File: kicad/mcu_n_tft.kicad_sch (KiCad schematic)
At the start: 14 parts, among them Q3 SS8050-G, Q4 SS8050-G, SW1 SW_MEC_5G, SW2 SW_MEC_5G, U4 ESP32-S3-Rx

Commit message: rework pcb
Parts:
- removed C10, C11, C12: 100n, Capacitor_SMD:C_0603_1608Metric, symbol Device:C
- removed Q3, Q4: SS8050-G, Package_TO_SOT_SMD:SOT-23, symbol z_ic:SS8050-G
- removed R28, R29, R32: 10k, Resistor_SMD:R_0603_1608Metric, symbol Device:R
- removed R30, R31, R33: 0R, Resistor_SMD:R_0603_1608Metric, symbol Device:R
- removed SW1, SW2: SW_MEC_5G, z_connector:PTS820J25MSMTRLFS, symbol z_connectors:SW_MEC_5G
- removed U4: ESP32-S3-Rx, z_ic:ESP32-S3-WROOM-1, symbol z_ic:ESP32-S3-Rx
- added J?: Conn_01x05, mylib_connector:Easy-On 51281-5, symbol Connector_Generic:Conn_01x05
- added J?: TC-2050, mylib_connector:TC-2050, symbol mylib_connectors:TC-2050
- added U4: BL654, mylib_ic:BL654, symbol mylib_ic:BL654
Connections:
- net +3V3: now also J?.1 (VCC), U4.25 (VDD_HV), U4.31 (VDD)
- net GND: now also J?.3 (GND), J?.5 (GND), U4.0 (GND), U4.23 (GND), U4.26 (GND), U4.33 (GND), U4.40 (GND), U4.43 (GND), U4.47 (GND), U4.52 (GND), U4.55 (GND), U4.58 (GND), U4.65 (GND), U4.66 (GND), U4.67 (GND), U4.68 (GND), U4.69 (GND), U4.70 (GND), U4.71 (GND)
- net PWR_PWM: now also U4.6 (P1.01)
- net PWR_PWM_INT: now also U4.5 (P1.03)
- net SCL: now also U4.2 (P1.04)
- net SDA: now also U4.4 (P1.02)
- net ~{INT}: now also U4.27 (P0.11)
- net ~{PD}: now also U4.22 (P0.14)
- new net: J?.2 (Pin_2), U4.59 (NFC_1)
- new net: J?.4 (Pin_4), U4.57 (NFC_2)
- new net +5V: U4.24 (VBUS)
- new net ADC_0: U4.50 (P0.02/AIN0)
- new net ADC_1: U4.49 (P0.03/AIN1)
- new net ADC_2: U4.34 (P0.04/AIN2)
- new net ADC_3: U4.39 (P0.05/AIN3)
- new net ADC_4: U4.46 (P0.28/AIN4)
- new net ADC_5: U4.48 (P0.29/AIN5)
- new net ADC_6: U4.45 (P0.30/AIN6)
- new net ADC_7: U4.44 (P0.31/AIN7)
- new net D+: U4.15 (D+)
- new net D-: U4.17 (D-)
- new net QSPI_CLK: U4.28 (P0.12)
- new net QSPI_IO0: U4.38 (P0.27)
- new net QSPI_IO1: U4.37 (P0.07)
- new net QSPI_IO2: U4.36 (P0.26)
- new net QSPI_IO3: U4.35 (P0.06)
- new net QSPI_~{CS}: U4.29 (P0.08)
- new net Reset: J?.10 (RESET), U4.19 (~{Reset})
- new net SWCLK: J?.4 (TCK/SWCLK), U4.3 (SWDCLK)
- new net SWDIO: J?.2 (TMS/SWDIO), U4.1 (SWDIO)
- new net SWO: J?.6 (TDO/SWO), U4.7 (P1.00)
- no-connect marks 13 -> 6

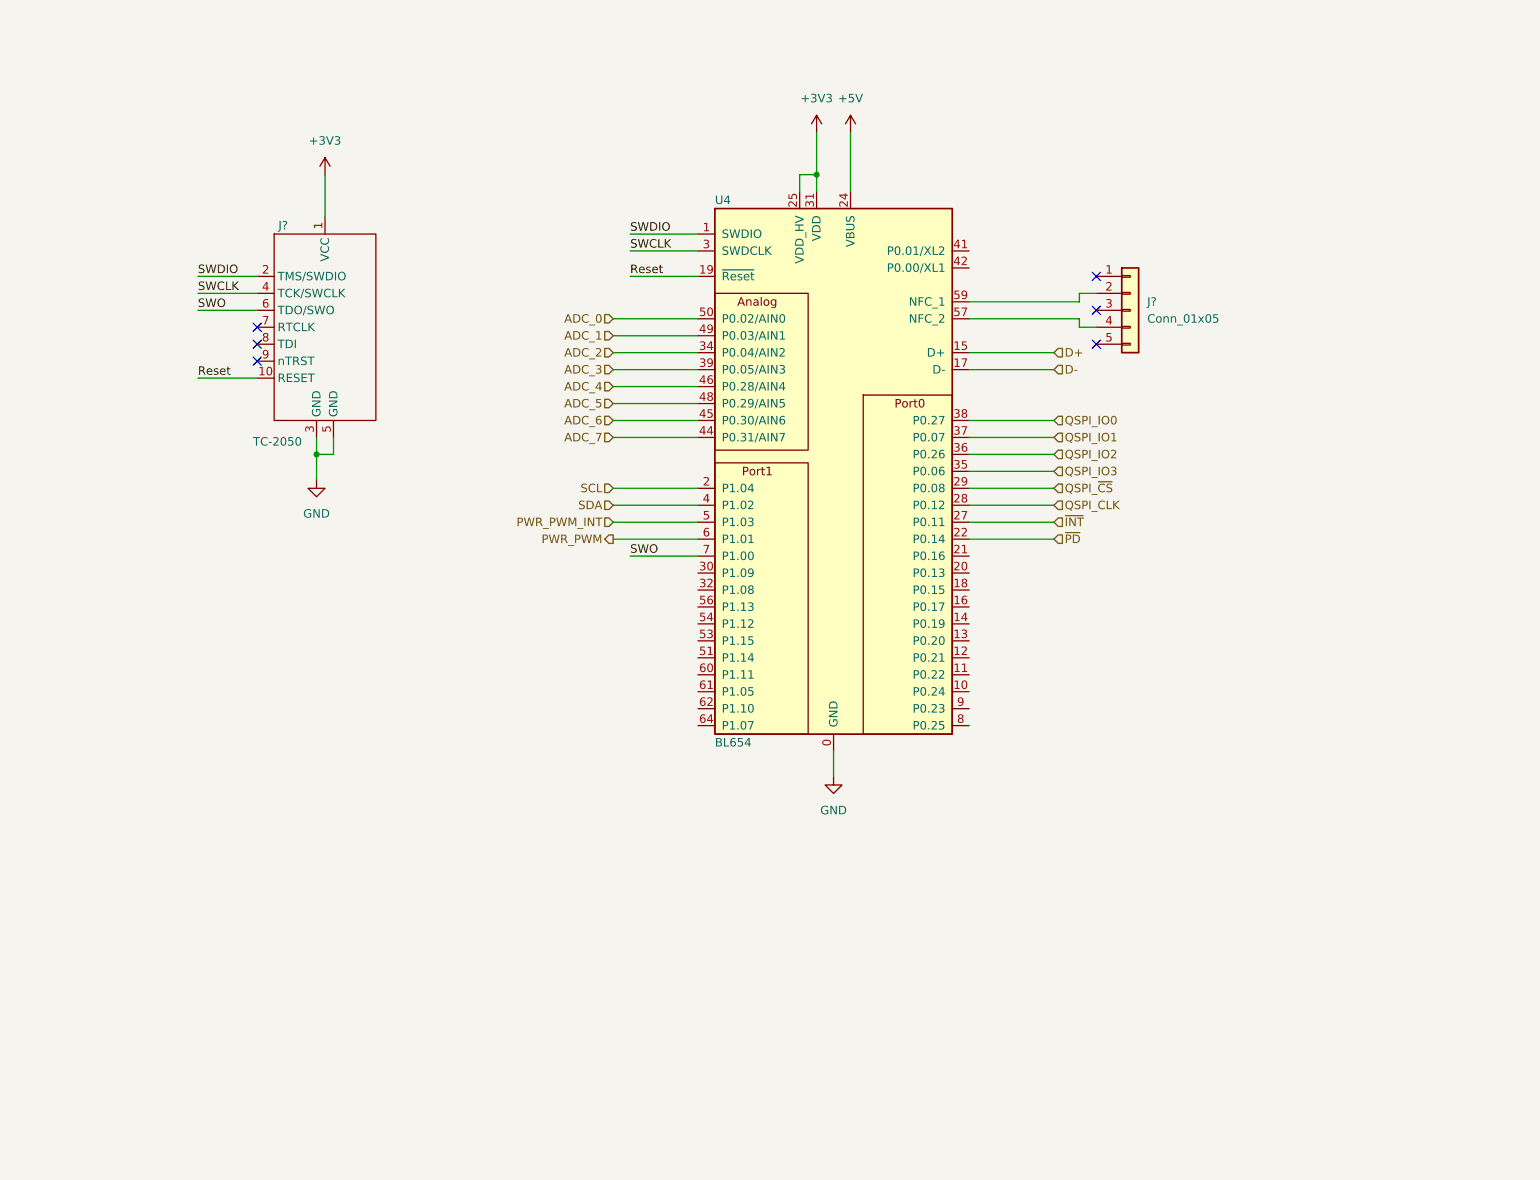
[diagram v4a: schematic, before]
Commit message: add all digikeys numbers to schematic
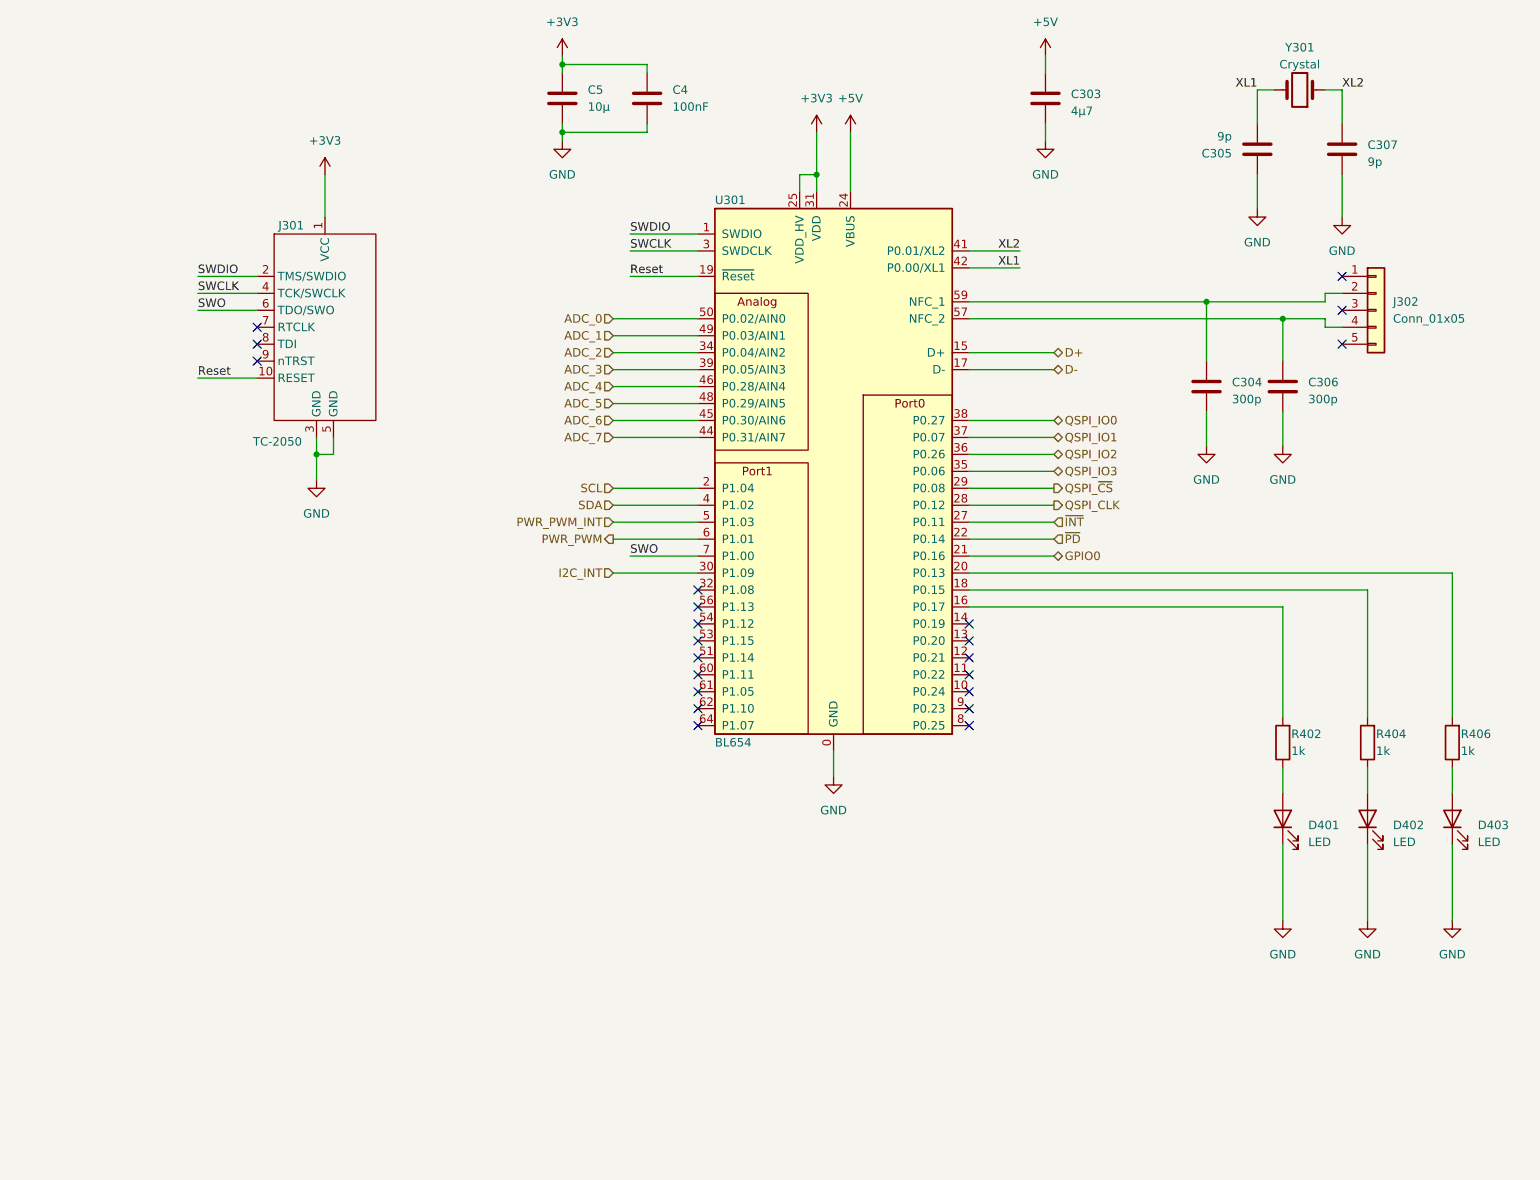
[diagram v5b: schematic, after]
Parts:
- added C303: 4µ7, Capacitor_SMD:C_0603_1608Metric, symbol Device:C
- added C304, C306: 300p, Capacitor_SMD:C_0603_1608Metric, symbol Device:C
- added C305, C307: 9p, Capacitor_SMD:C_0603_1608Metric, symbol Device:C
- added C4: 100nF, Capacitor_SMD:C_0603_1608Metric, symbol Device:C
- added C5: 10µ, Capacitor_SMD:C_0603_1608Metric, symbol Device:C
- added D401, D402, D403: LED, LED_SMD:LED_0603_1608Metric, symbol Device:LED
- added R402, R404, R406: 1k, Resistor_SMD:R_0603_1608Metric, symbol Device:R
- added Y301: Crystal, mylib_ic:CM8V-T1A-2Pin_2.0x1.2mm, symbol Device:Crystal
- J302: renamed from J?; Digikey (none) -> 900-0512810598CT-ND
- gave numbers to parts that had none: 1
- renumbered U4 to U301
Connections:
- net +3V3: now also C4.1, C5.1
- net +5V: now also C303.1
- net GND: now also C303.2, C304.2, C305.1, C306.2, C307.2, C4.2, C5.2, D401.1 (K), D402.1 (K), D403.1 (K)
- net at J302.2 (Pin_2), U301.59 (NFC_1): now also C304.1
- net at J302.4 (Pin_4), U301.57 (NFC_2): now also C306.1
- net at U301.16 (P0.17): now also R402.2
- net at U301.18 (P0.15): now also R404.2
- net at U301.20 (P0.13): now also R406.2
- net GPIO0: now reaches U301.21 (P0.16)
- net I2C_INT: now reaches U301.30 (P1.09)
- net XL2: now reaches U301.41 (P0.01/XL2)
- net XL2: now also C307.1, Y301.1
- net XL1: now reaches U301.42 (P0.00/XL1)
- net XL1: now also C305.2, Y301.2
- new net: D403.2 (A), R406.1
- new net: D402.2 (A), R404.1
- new net: D401.2 (A), R402.1
- no-connect marks 6 -> 22
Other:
- moved on the sheet: J302

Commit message: wip
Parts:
- renumbered C305 to C304, C307 to C305, C304 to C306, C306 to C307, J302 to J301, J301 to J302

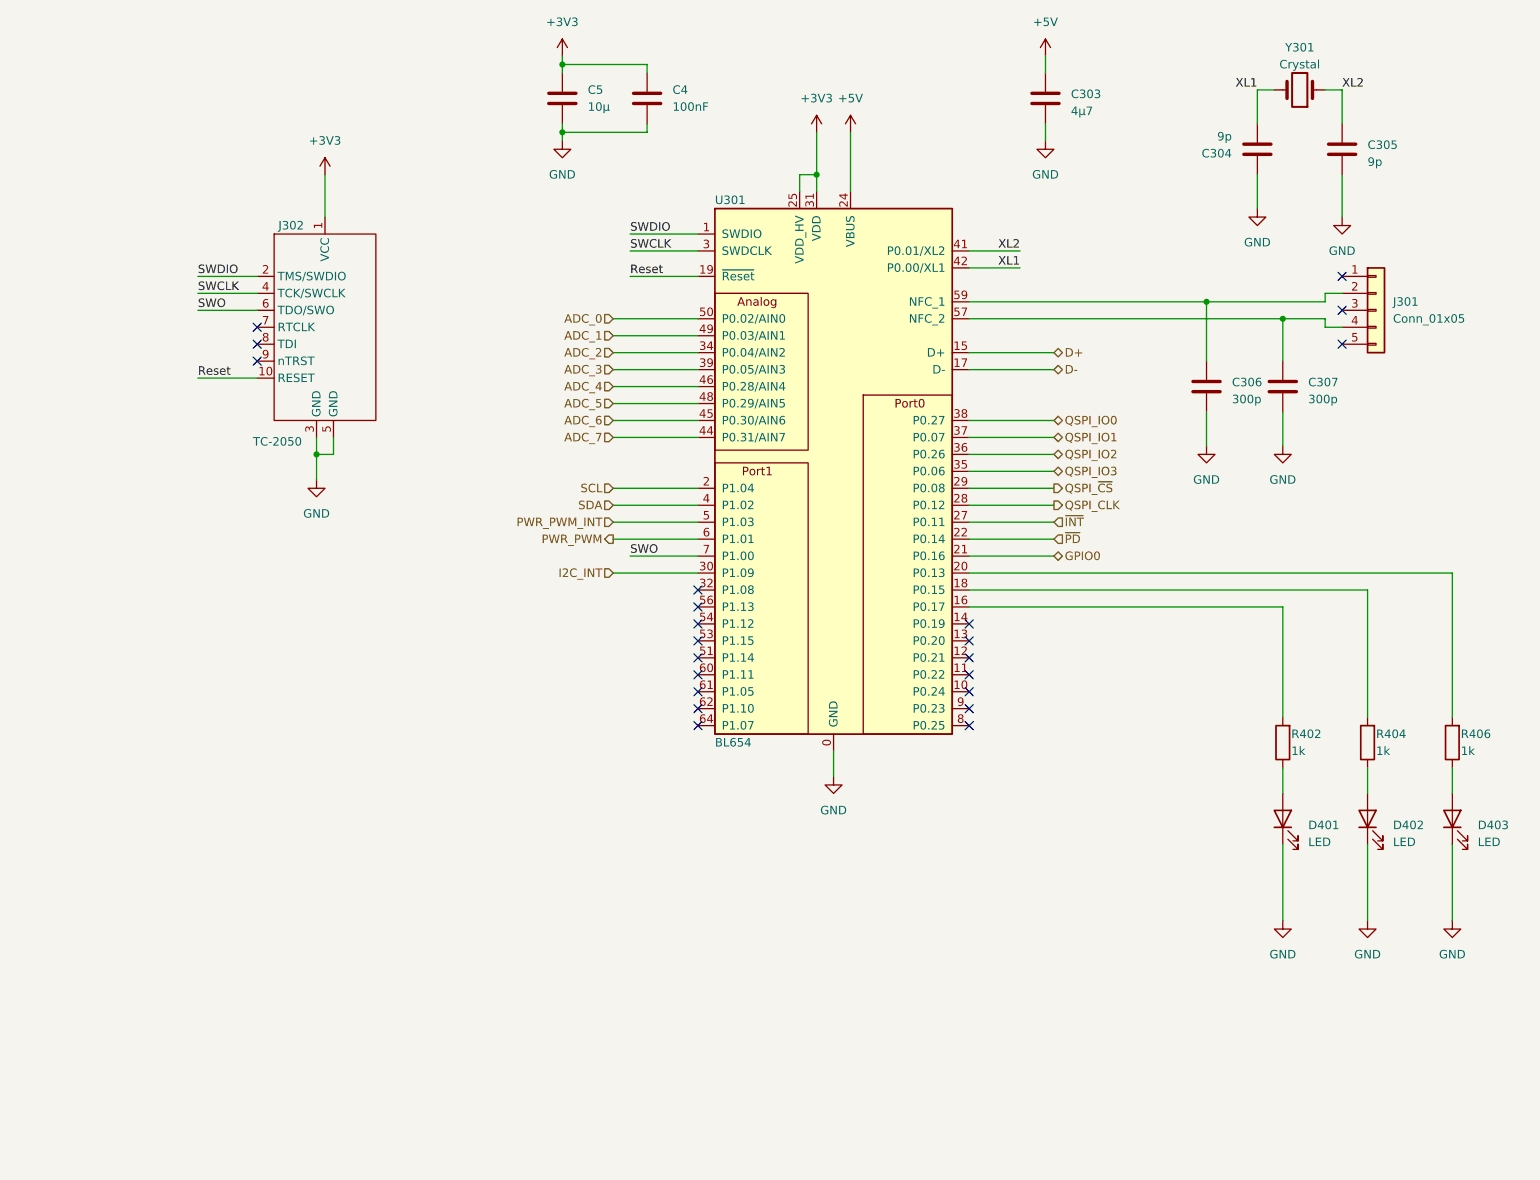
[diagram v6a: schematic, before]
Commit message: add nrf52840 board
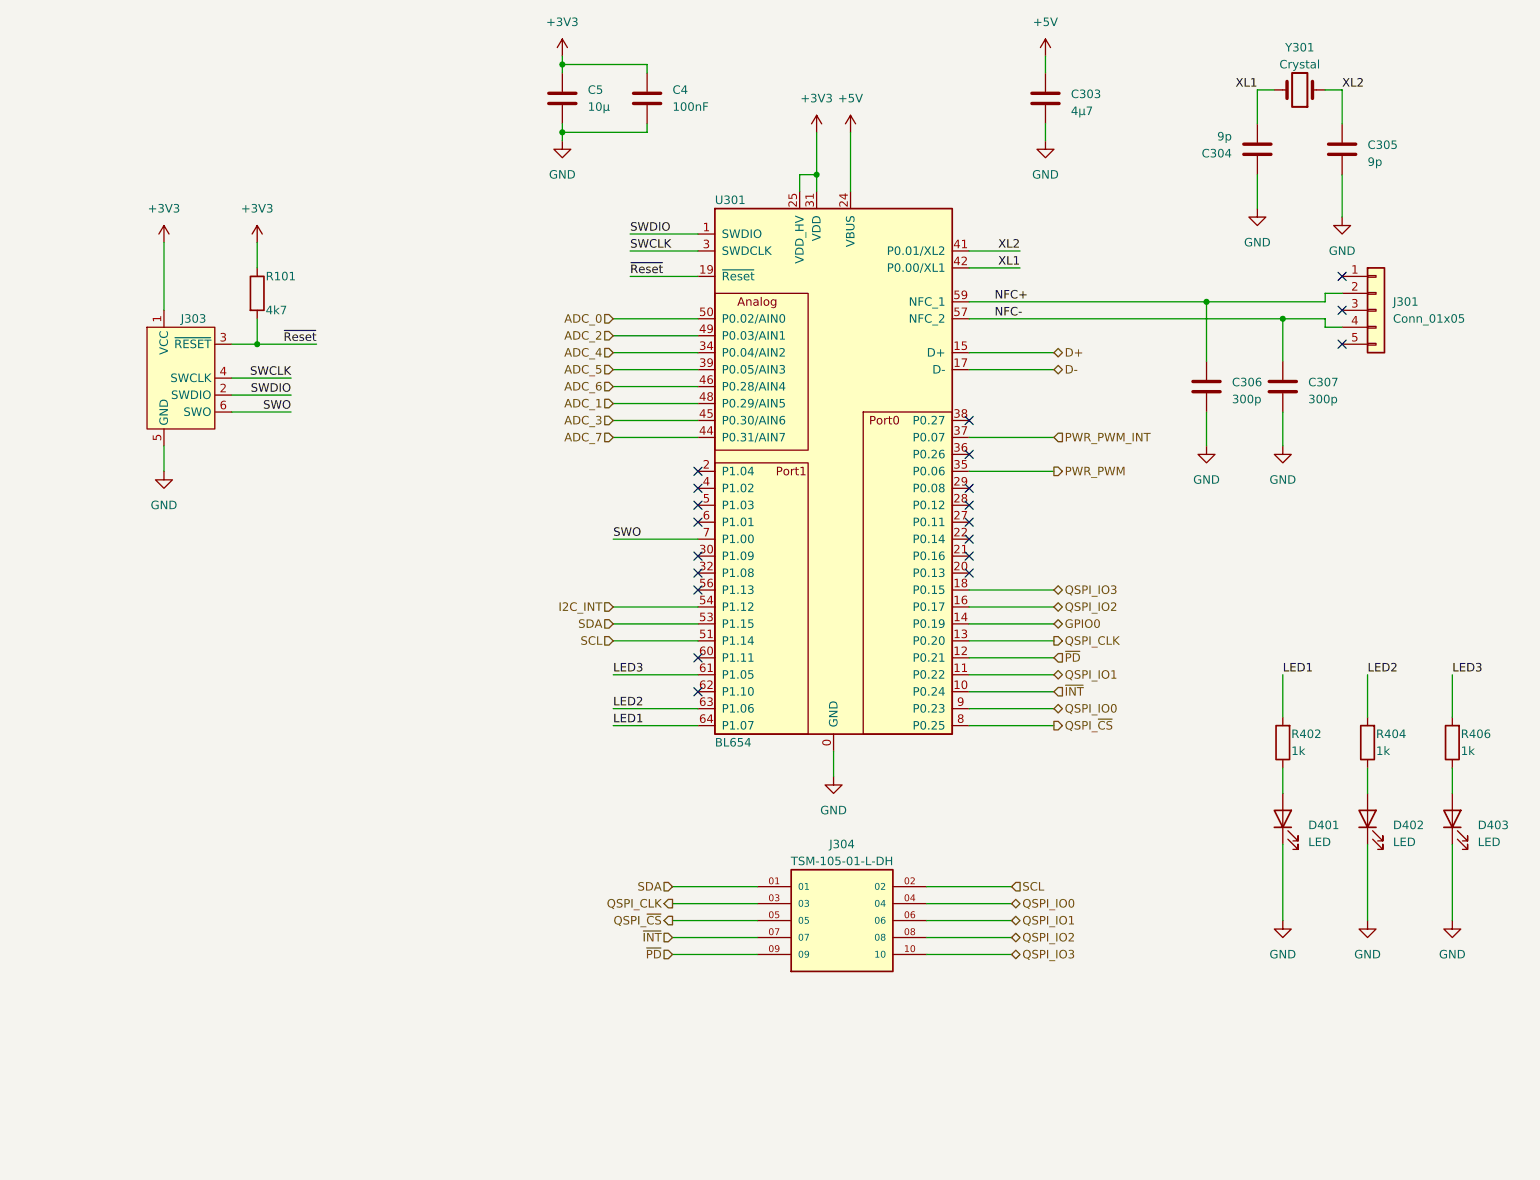
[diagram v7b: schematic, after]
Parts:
- removed J302: TC-2050, mylib_connector:TC-2050, symbol mylib_connectors:TC-2050
- added J303: Conn_ARM_SWD_TagConnect_TC2030, Connector:Tag-Connect_TC2030-IDC-FP_2x03_P1.27mm_Vertical, symbol Connector:Conn_ARM_SWD_TagConnect_TC2030
- added J304: TSM-105-01-L-DH, mylib_connector:SAMTEC_TSM-105-01-L-DH, symbol mylib_connectors:TSM-105-01-L-DH
- added R101: 4k7, Resistor_SMD:R_0603_1608Metric, symbol Device:R
- C303: Digikey (none) -> 478-06033D475KAT2ACT-ND
- U301: footprint mylib_ic:BL654 -> mylib_ic:BL654-00001; Digikey (none) -> 451-00001CT-ND
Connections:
- net +3V3: now also J303.1 (VCC), R101.1
- net ADC_1: now also U301.48 (P0.29/AIN5); no longer U301.49 (P0.03/AIN1)
- net ADC_2: now also U301.49 (P0.03/AIN1); no longer U301.34 (P0.04/AIN2)
- net ADC_3: now also U301.45 (P0.30/AIN6); no longer U301.39 (P0.05/AIN3)
- net ADC_4: now also U301.34 (P0.04/AIN2); no longer U301.46 (P0.28/AIN4)
- net ADC_5: now also U301.39 (P0.05/AIN3); no longer U301.48 (P0.29/AIN5)
- net ADC_6: now also U301.46 (P0.28/AIN4); no longer U301.45 (P0.30/AIN6)
- net GND: now also J303.5 (GND)
- net GPIO0: now also U301.14 (P0.19); no longer U301.21 (P0.16)
- net I2C_INT: now also U301.54 (P1.12); no longer U301.30 (P1.09)
- net PWR_PWM: now also U301.35 (P0.06); no longer U301.6 (P1.01)
- net PWR_PWM_INT: now also U301.37 (P0.07); no longer U301.5 (P1.03)
- net QSPI_CLK: now also U301.13 (P0.20), J304.03; no longer U301.28 (P0.12)
- net QSPI_IO0: now also U301.9 (P0.23), J304.04; no longer U301.38 (P0.27)
- net QSPI_IO1: now also U301.11 (P0.22), J304.06; no longer U301.37 (P0.07)
- net QSPI_IO2: now also U301.16 (P0.17), J304.08; no longer U301.36 (P0.26)
- net QSPI_IO3: now also U301.18 (P0.15), J304.10; no longer U301.35 (P0.06)
- net QSPI_~{CS}: now also U301.8 (P0.25), J304.05; no longer U301.29 (P0.08)
- net SCL: now also U301.51 (P1.14), J304.02; no longer U301.2 (P1.04)
- net SDA: now also U301.53 (P1.15), J304.01; no longer U301.4 (P1.02)
- net SWCLK: now also J303.4 (SWCLK)
- net SWDIO: now also J303.2 (SWDIO)
- net SWO: now also J303.6 (SWO)
- net ~{INT}: now also U301.10 (P0.24), J304.07; no longer U301.27 (P0.11)
- net ~{PD}: now also U301.12 (P0.21), J304.09; no longer U301.22 (P0.14)
- net NFC-: now reaches C307.1, J301.4 (Pin_4), U301.57 (NFC_2)
- net NFC+: now reaches C306.1, J301.2 (Pin_2), U301.59 (NFC_1)
- net at U301.20 (P0.13): no longer R406.2
- net LED1: now reaches R402.2
- net LED1: now also U301.64 (P1.07); no longer U301.16 (P0.17)
- net LED2: now reaches R404.2
- net LED2: now also U301.63 (P1.06); no longer U301.18 (P0.15)
- net LED3: now reaches U301.61 (P1.05)
- net LED3: now also R406.2
- net Reset renamed ~{Reset}
- net ~{Reset}: now also J303.3 (~{RESET}), R101.2
- no-connect marks 22 -> 20
